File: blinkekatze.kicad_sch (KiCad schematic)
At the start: 8 parts, among them J1 Power key

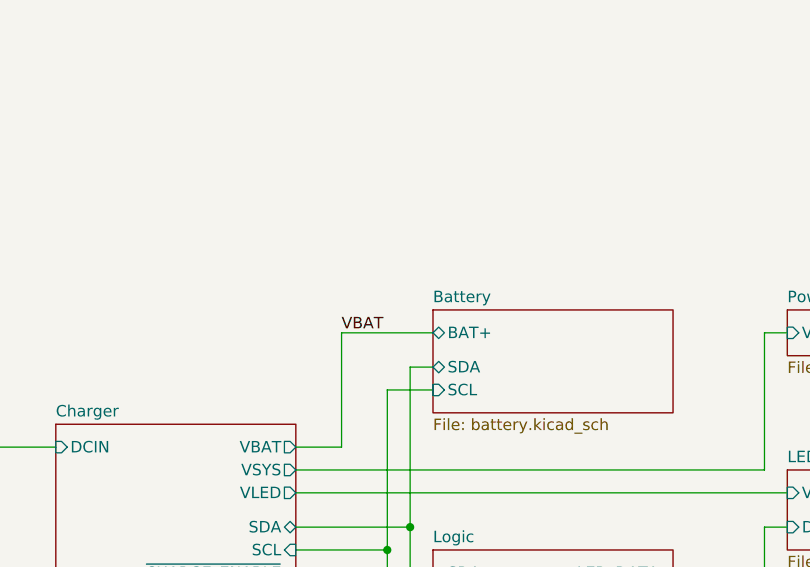
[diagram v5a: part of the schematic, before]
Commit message: Add I2C test connector
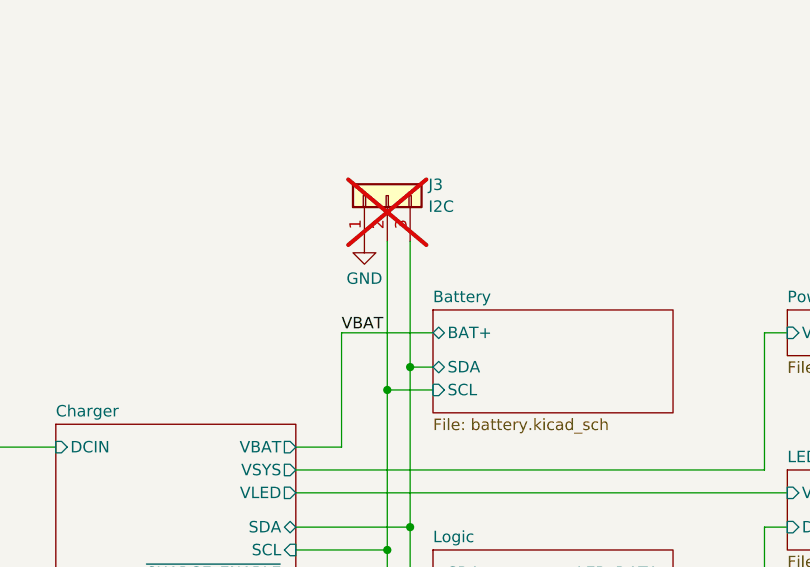
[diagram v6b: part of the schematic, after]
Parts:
- added J3: I2C, Connector_PinHeader_2.54mm:PinHeader_1x03_P2.54mm_Vertical, symbol Connector_Generic:Conn_01x03
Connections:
- net Battery/SCL: now also J3.2 (Pin_2)
- net Battery/SDA: now also J3.3 (Pin_3)
- new net GND: J3.1 (Pin_1)
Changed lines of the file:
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@@
   (junction (at 139.7 101.6) (diameter 0) (color 0 0 0 0)
   )
+  (junction (at 137.16 86.36) (diameter 0) (color 0 0 0 0)
+  )
+  (junction (at 139.7 83.82) (diameter 0) (color 0 0 0 0)
+  )
   (junction (at 137.16 104.14) (diameter 0) (color 0 0 0 0)
   )
@@
     (stroke (width 0) (type default))
   )
+  (wire (pts (xy 137.16 69.85) (xy 137.16 86.36))
+    (stroke (width 0) (type default))
+  )
   (wire (pts (xy 127 130.81) (xy 129.54 130.81))
     (stroke (width 0) (type default))
@@
   )
   (wire (pts (xy 127 106.68) (xy 134.62 106.68))
+    (stroke (width 0) (type default))
+  )
+  (wire (pts (xy 139.7 69.85) (xy 139.7 83.82))
     (stroke (width 0) (type default))
   )
@@
         )
       )
+    )
+  )
+  (symbol (lib_id "Connector_Generic:Conn_01x03") (at 137.16 64.77 90) (unit 1)
+    (in_bom no) (on_board yes) (dnp yes) (fields_autoplaced)
+    (property "Reference" "J3" (at 141.732 63.5579 90)
+      (effects (font (size 1.27 1.27)) (justify right))
+    )
+    (property "Value" "I2C" (at 141.732 65.9821 90)
+      (effects (font (size 1.27 1.27)) (justify right))
+    )
+    (property "Footprint" "Connector_PinHeader_2.54mm:PinHeader_1x03_P2.54mm_Vertical" (at 137.16 64.77 0)
+      (effects (font (size 1.27 1.27)) hide)
+    )
+    (property "Datasheet" "~" (at 137.16 64.77 0)
+      (effects (font (size 1.27 1.27)) hide)
+    )
+    (pin "1")
+    (pin "2")
+    (pin "3")
+    (instances
+      (project "blinkekatze"
+        (path "/20b2a5b0-0a80-4b97-84d4-d5290b2926e5"
+          (reference "J3") (unit 1)
+        )
+      )
+    )
+  )
+  (symbol (lib_id "power:GND") (at 134.62 69.85 0) (unit 1)
+    (in_bom yes) (on_board yes) (dnp no) (fields_autoplaced)
+    (property "Reference" "#PWR064" (at 134.62 76.2 0)
+      (effects (font (size 1.27 1.27)) hide)
+    )
+    (property "Value" "GND" (at 134.62 73.9831 0)
+      (effects (font (size 1.27 1.27)))
+    )
+    (property "Footprint" "" (at 134.62 69.85 0)
+      (effects (font (size 1.27 1.27)) hide)
+    )
+    (property "Datasheet" "" (at 134.62 69.85 0)
+      (effects (font (size 1.27 1.27)) hide)
+    )
+    (pin "1")
+    (instances
+      (project "blinkekatze"
+        (path "/20b2a5b0-0a80-4b97-84d4-d5290b2926e5"
+          (reference "#PWR064") (unit 1)
+        )
+      )

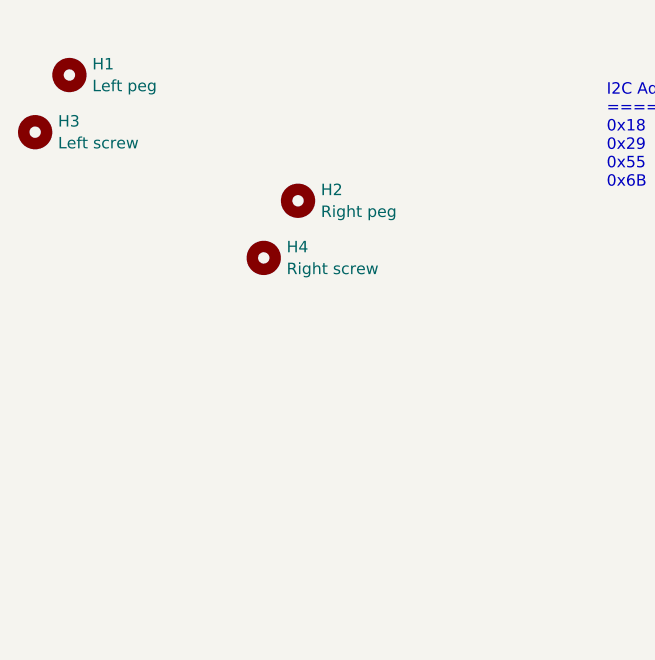
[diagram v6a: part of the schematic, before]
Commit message: Add additional mounting holes for micro USB cat nightlight variant
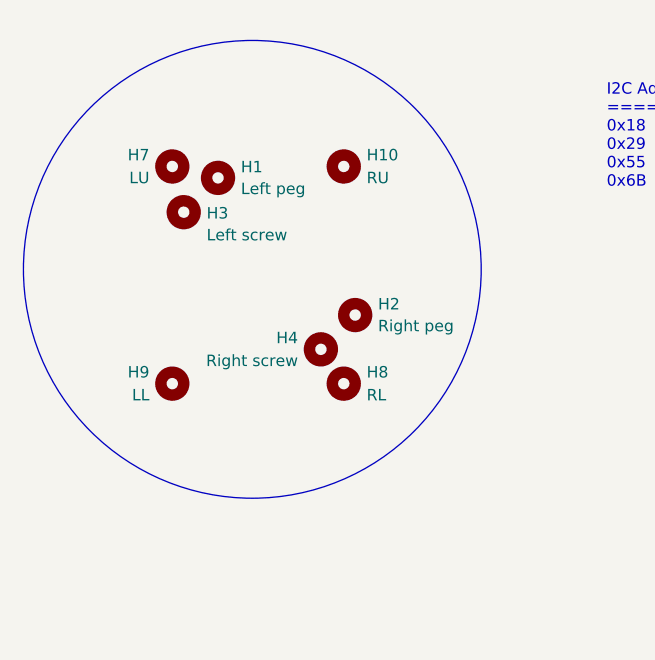
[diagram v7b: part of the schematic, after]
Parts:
- added H10: RU, MountingHole:MountingHole_2.5mm, symbol Mechanical:MountingHole
- added H7: LU, MountingHole:MountingHole_2.5mm, symbol Mechanical:MountingHole
- added H8: RL, MountingHole:MountingHole_2.5mm, symbol Mechanical:MountingHole
- added H9: LL, MountingHole:MountingHole_2.5mm, symbol Mechanical:MountingHole
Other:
- moved on the sheet: H1, H2, H3, H4
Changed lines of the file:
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@@
     (stroke (width 0) (type default))
+  )
+  (circle (center 45.72 41.91) (radius 25.4317)
+    (stroke (width 0) (type default) (color 194 194 0 1))
+    (fill (type none))
   )
   (text "I2C Addresses\n================\n0x18   LIS3D\n0x29   303ALS-01\n0x55   BQ27546\n0x6B   BQ24295\n"
@@
     (effects (font (size 1.27 1.27)) (justify left bottom))
   )
-  (symbol (lib_id "Mechanical:MountingHole") (at 25.4 20.32 0) (unit 1)
+  (symbol (lib_id "Mechanical:MountingHole") (at 36.83 54.61 0) (unit 1)
+    (in_bom no) (on_board yes) (dnp no)
+    (property "Reference" "H9" (at 34.29 53.34 0)
+      (effects (font (size 1.27 1.27)) (justify right))
+    )
+    (property "Value" "LL" (at 34.29 55.88 0)
+      (effects (font (size 1.27 1.27)) (justify right))
+    )
+    (property "Footprint" "MountingHole:MountingHole_2.5mm" (at 36.83 54.61 0)
+      (effects (font (size 1.27 1.27)) hide)
+    )
+    (property "Datasheet" "~" (at 36.83 54.61 0)
+      (effects (font (size 1.27 1.27)) hide)
+    )
+    (instances
+      (project "blinkekatze"
+        (path "/20b2a5b0-0a80-4b97-84d4-d5290b2926e5"
+          (reference "H9") (unit 1)
+        )
+      )
+    )
+  )
+  (symbol (lib_id "Mechanical:MountingHole") (at 55.88 54.61 0) (unit 1)
+    (in_bom no) (on_board yes) (dnp no)
+    (property "Reference" "H8" (at 58.42 53.34 0)
+      (effects (font (size 1.27 1.27)) (justify left))
+    )
+    (property "Value" "RL" (at 58.42 55.88 0)
+      (effects (font (size 1.27 1.27)) (justify left))
+    )
+    (property "Footprint" "MountingHole:MountingHole_2.5mm" (at 55.88 54.61 0)
+      (effects (font (size 1.27 1.27)) hide)
+    )
+    (property "Datasheet" "~" (at 55.88 54.61 0)
+      (effects (font (size 1.27 1.27)) hide)
+    )
+    (instances
+      (project "blinkekatze"
+        (path "/20b2a5b0-0a80-4b97-84d4-d5290b2926e5"
+          (reference "H8") (unit 1)
+        )
+      )
+    )
+  )
+  (symbol (lib_id "Mechanical:MountingHole") (at 41.91 31.75 0) (unit 1)
     (in_bom no) (on_board yes) (dnp no) (fields_autoplaced)
-    (property "Reference" "H1" (at 27.94 19.1079 0)
-      (effects (font (size 1.27 1.27)) (justify left))
-    )
-    (property "Value" "Left peg" (at 27.94 21.5321 0)
-      (effects (font (size 1.27 1.27)) (justify left))
-    )
-    (property "Footprint" "MountingHole:MountingHole_2.1mm" (at 25.4 20.32 0)
-      (effects (font (size 1.27 1.27)) hide)
-    )
-    (property "Datasheet" "~" (at 25.4 20.32 0)
+    (property "Reference" "H1" (at 44.45 30.5379 0)
+      (effects (font (size 1.27 1.27)) (justify left))
+    )
+    (property "Value" "Left peg" (at 44.45 32.9621 0)
+      (effects (font (size 1.27 1.27)) (justify left))
+    )
+    (property "Footprint" "MountingHole:MountingHole_2.1mm" (at 41.91 31.75 0)
+      (effects (font (size 1.27 1.27)) hide)
+    )
+    (property "Datasheet" "~" (at 41.91 31.75 0)
       (effects (font (size 1.27 1.27)) hide)
     )
@@
     )
   )
-  (symbol (lib_id "Mechanical:MountingHole") (at 46.99 40.64 0) (unit 1)
+  (symbol (lib_id "Mechanical:MountingHole") (at 53.34 50.8 0) (unit 1)
+    (in_bom no) (on_board yes) (dnp no)
+    (property "Reference" "H4" (at 50.8 49.53 0)
+      (effects (font (size 1.27 1.27)) (justify right))
+    )
+    (property "Value" "Right screw" (at 50.8 52.07 0)
+      (effects (font (size 1.27 1.27)) (justify right))
+    )
+    (property "Footprint" "MountingHole:MountingHole_2.5mm" (at 53.34 50.8 0)
+      (effects (font (size 1.27 1.27)) hide)
+    )
+    (property "Datasheet" "~" (at 53.34 50.8 0)
+      (effects (font (size 1.27 1.27)) hide)
+    )
+    (instances
+      (project "blinkekatze"
+        (path "/20b2a5b0-0a80-4b97-84d4-d5290b2926e5"
+          (reference "H4") (unit 1)
+        )
+      )
+    )
+  )
+  (symbol (lib_id "Mechanical:MountingHole") (at 57.15 46.99 0) (unit 1)
     (in_bom no) (on_board yes) (dnp no) (fields_autoplaced)
-    (property "Reference" "H4" (at 49.53 39.4279 0)
-      (effects (font (size 1.27 1.27)) (justify left))
-    )
-    (property "Value" "Right screw" (at 49.53 41.8521 0)
-      (effects (font (size 1.27 1.27)) (justify left))
-    )
-    (property "Footprint" "MountingHole:MountingHole_2.5mm" (at 46.99 40.64 0)
-      (effects (font (size 1.27 1.27)) hide)
-    )
-    (property "Datasheet" "~" (at 46.99 40.64 0)
-      (effects (font (size 1.27 1.27)) hide)
-    )
-    (instances
-      (project "blinkekatze"
-        (path "/20b2a5b0-0a80-4b97-84d4-d5290b2926e5"
-          (reference "H4") (unit 1)
-        )
-      )
-    )
-  )
-  (symbol (lib_id "Mechanical:MountingHole") (at 50.8 34.29 0) (unit 1)
-    (in_bom no) (on_board yes) (dnp no) (fields_autoplaced)
-    (property "Reference" "H2" (at 53.34 33.0779 0)
-      (effects (font (size 1.27 1.27)) (justify left))
-    )
-    (property "Value" "Right peg" (at 53.34 35.5021 0)
-      (effects (font (size 1.27 1.27)) (justify left))
-    )
-    (property "Footprint" "MountingHole:MountingHole_2.1mm" (at 50.8 34.29 0)
-      (effects (font (size 1.27 1.27)) hide)
-    )
-    (property "Datasheet" "~" (at 50.8 34.29 0)
+    (property "Reference" "H2" (at 59.69 45.7779 0)
+      (effects (font (size 1.27 1.27)) (justify left))
+    )
+    (property "Value" "Right peg" (at 59.69 48.2021 0)
+      (effects (font (size 1.27 1.27)) (justify left))
+    )
+    (property "Footprint" "MountingHole:MountingHole_2.1mm" (at 57.15 46.99 0)
+      (effects (font (size 1.27 1.27)) hide)
+    )
+    (property "Datasheet" "~" (at 57.15 46.99 0)
       (effects (font (size 1.27 1.27)) hide)
     )
@@
     )
   )
-  (symbol (lib_id "Mechanical:MountingHole") (at 21.59 26.67 0) (unit 1)
-    (in_bom no) (on_board yes) (dnp no) (fields_autoplaced)
-    (property "Reference" "H3" (at 24.13 25.4579 0)
-      (effects (font (size 1.27 1.27)) (justify left))
-    )
-    (property "Value" "Left screw" (at 24.13 27.8821 0)
-      (effects (font (size 1.27 1.27)) (justify left))
-    )
-    (property "Footprint" "MountingHole:MountingHole_2.5mm" (at 21.59 26.67 0)
-      (effects (font (size 1.27 1.27)) hide)
-    )
-    (property "Datasheet" "~" (at 21.59 26.67 0)
+  (symbol (lib_id "Mechanical:MountingHole") (at 38.1 35.56 0) (unit 1)
+    (in_bom no) (on_board yes) (dnp no)
+    (property "Reference" "H3" (at 40.64 35.6758 0)
+      (effects (font (size 1.27 1.27)) (justify left))
+    )
+    (property "Value" "Left screw" (at 40.64 38.1 0)
+      (effects (font (size 1.27 1.27)) (justify left))
+    )
+    (property "Footprint" "MountingHole:MountingHole_2.5mm" (at 38.1 35.56 0)
+      (effects (font (size 1.27 1.27)) hide)
+    )
+    (property "Datasheet" "~" (at 38.1 35.56 0)
       (effects (font (size 1.27 1.27)) hide)
     )
@@
         )
       )
+    )
+  )
+  (symbol (lib_id "Mechanical:MountingHole") (at 36.83 30.48 0) (unit 1)
+    (in_bom no) (on_board yes) (dnp no)
+    (property "Reference" "H7" (at 34.29 29.21 0)
+      (effects (font (size 1.27 1.27)) (justify right))
+    )
+    (property "Value" "LU" (at 34.29 31.75 0)
+      (effects (font (size 1.27 1.27)) (justify right))
+    )
+    (property "Footprint" "MountingHole:MountingHole_2.5mm" (at 36.83 30.48 0)
+      (effects (font (size 1.27 1.27)) hide)
+    )
+    (property "Datasheet" "~" (at 36.83 30.48 0)
+      (effects (font (size 1.27 1.27)) hide)
+    )
+    (instances
+      (project "blinkekatze"
+        (path "/20b2a5b0-0a80-4b97-84d4-d5290b2926e5"
+          (reference "H7") (unit 1)
+        )
+      )
+    )
+  )
+  (symbol (lib_id "Mechanical:MountingHole") (at 55.88 30.48 0) (unit 1)
+    (in_bom no) (on_board yes) (dnp no)
+    (property "Reference" "H10" (at 58.42 29.21 0)
+      (effects (font (size 1.27 1.27)) (justify left))
+    )
+    (property "Value" "RU" (at 58.42 31.75 0)
+      (effects (font (size 1.27 1.27)) (justify left))
+    )
+    (property "Footprint" "MountingHole:MountingHole_2.5mm" (at 55.88 30.48 0)
+      (effects (font (size 1.27 1.27)) hide)
+    )
+    (property "Datasheet" "~" (at 55.88 30.48 0)
+      (effects (font (size 1.27 1.27)) hide)
+    )
+    (instances
+      (project "blinkekatze"
+        (path "/20b2a5b0-0a80-4b97-84d4-d5290b2926e5"
+          (reference "H10") (unit 1)
+        )
+      )

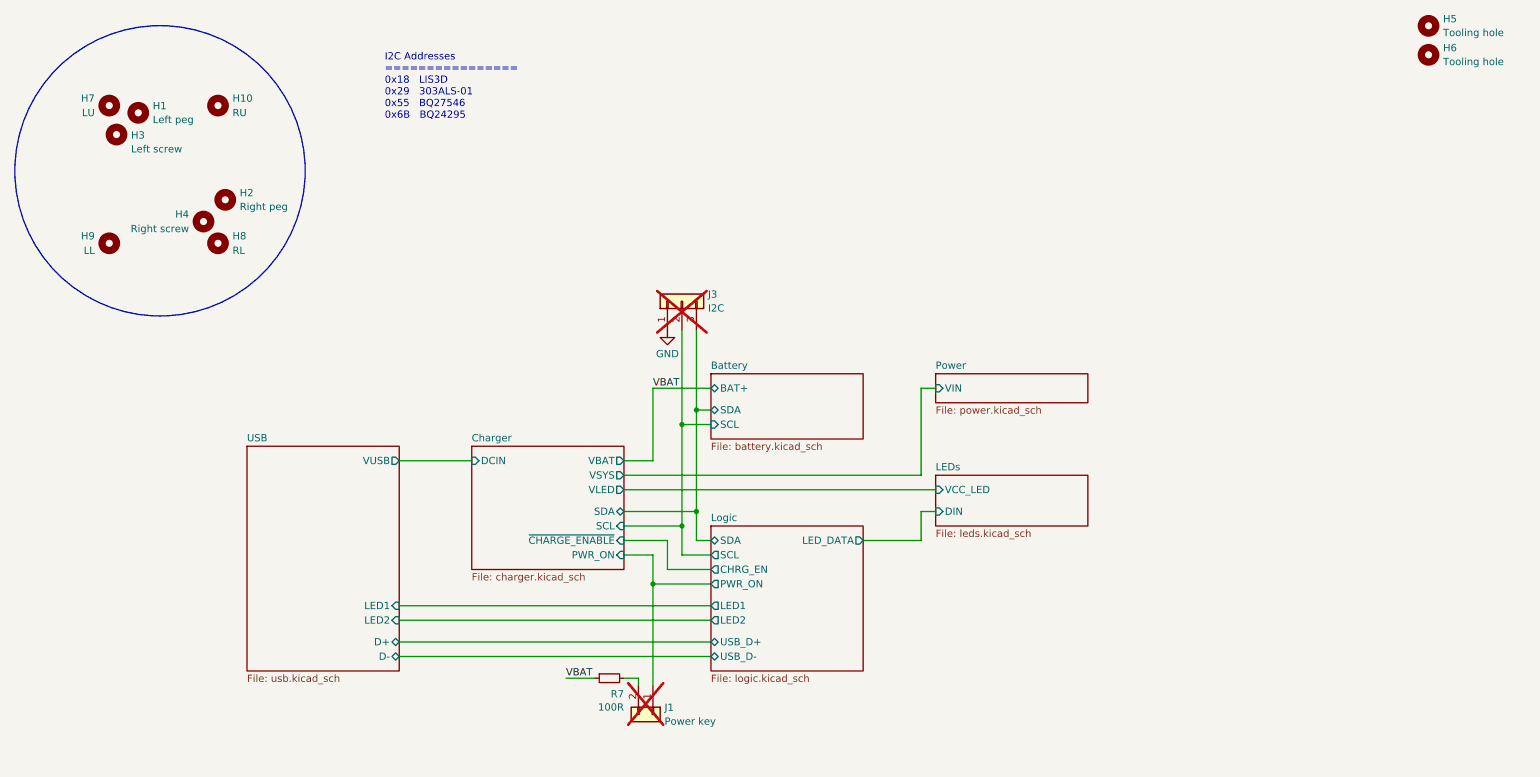
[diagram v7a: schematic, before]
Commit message: Relayout board to fit constraints of Micro USB Blinkekatzen
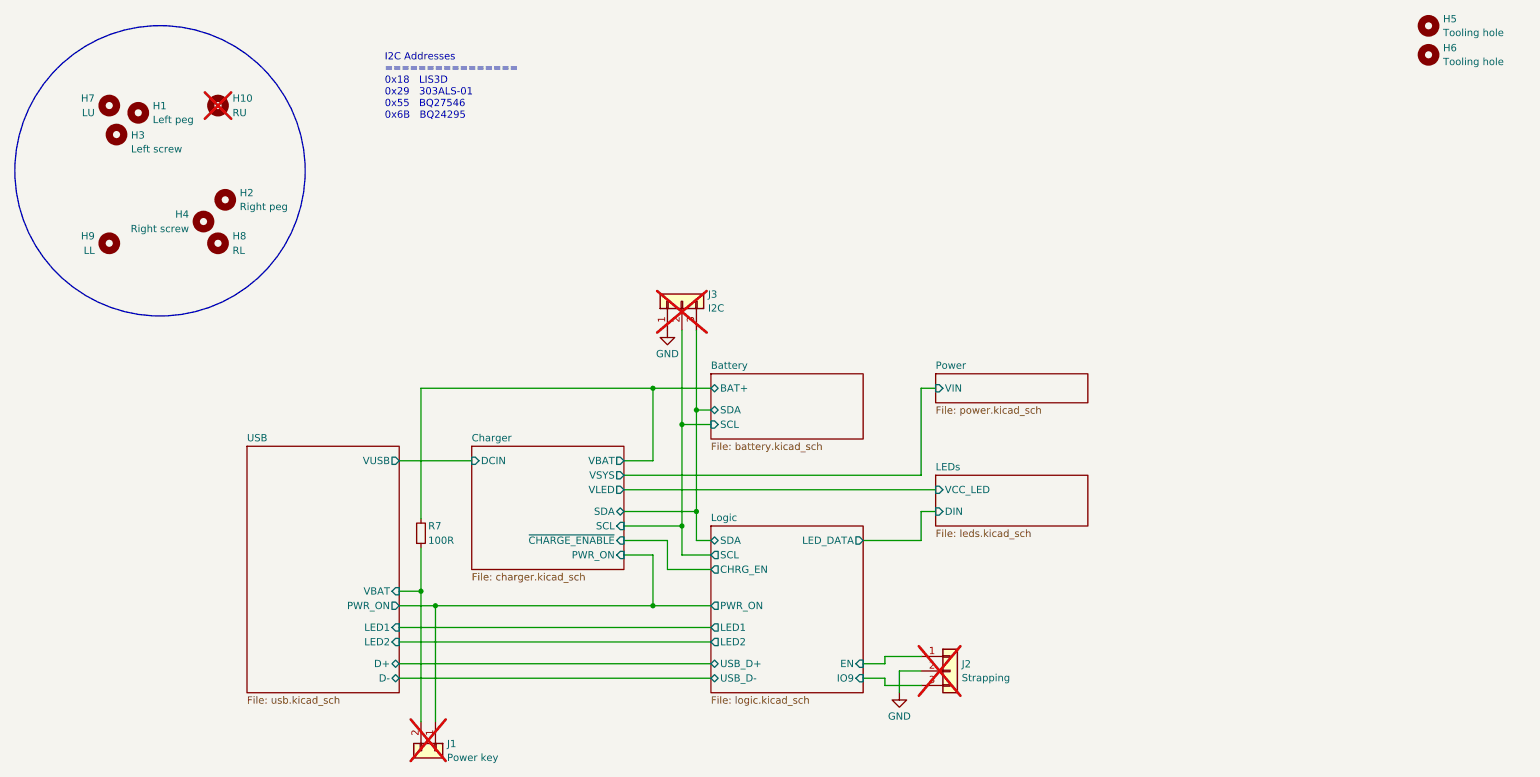
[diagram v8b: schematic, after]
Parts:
- added J2: Strapping, Connector_PinHeader_2.54mm:PinHeader_1x03_P2.54mm_Vertical, symbol Connector_Generic:Conn_01x03
- H10: now not fitted
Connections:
- net GND: now also J2.2 (Pin_2)
- net Battery/BAT+: now reaches R7.2
- net Battery/BAT+: no longer J1.2 (Pin_2)
- net VBAT renamed USB/VBAT
- net USB/VBAT: now also J1.2 (Pin_2)
- new net Logic/EN: J2.1 (Pin_1)
- new net Logic/IO9: J2.3 (Pin_3)
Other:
- sheet Logic ports: added EN, IO9; removed none
- sheet USB ports: added PWR_ON, VBAT; removed none
- moved on the sheet: J1, R7
